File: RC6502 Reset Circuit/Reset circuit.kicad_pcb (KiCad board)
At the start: 2 copper layers, 99.1 x 33 mm, 12 parts, among them J1 CONN_01X39, J2 XTAL Enable, SW1 RESET, U1 NE555, U2 74LS04, X1 1MHz

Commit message: Exported files
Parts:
- added C4: 100nF, Capacitors_THT:C_Disc_D3.0mm_W1.6mm_P2.50mm, F.Cu at (119.4, 139.1)
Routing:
- net VCC: track 149.8 -> 178.2 mm
- net GND: track 155.0 -> 158.1 mm
- net RESET: track 81.2 -> 83.5 mm

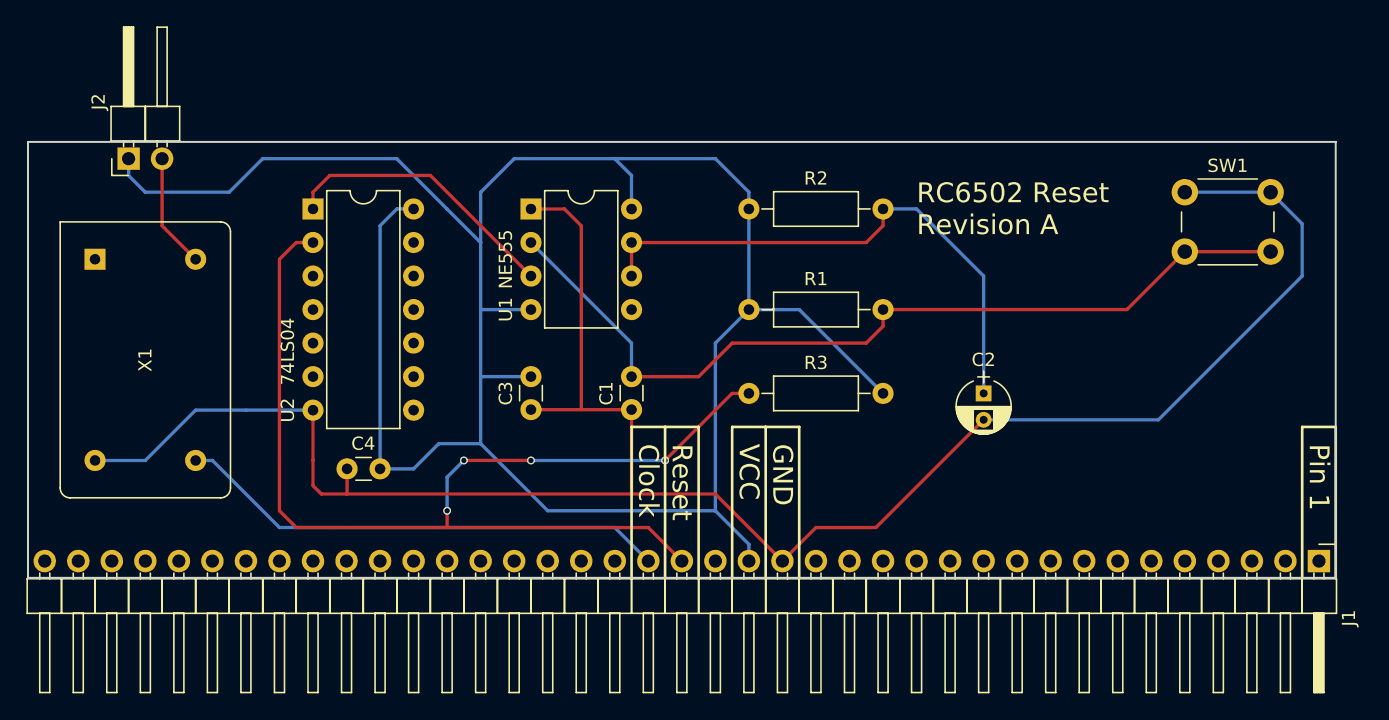
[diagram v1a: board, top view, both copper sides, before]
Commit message: Reset circuit revision B
Fixed floating inputs on hex inverter (needed when using HCT), added 74HCT74 in order to allow clock division by 2 and 4 (in case missing matching TTL quartz crystal or want even slower clock than stock).
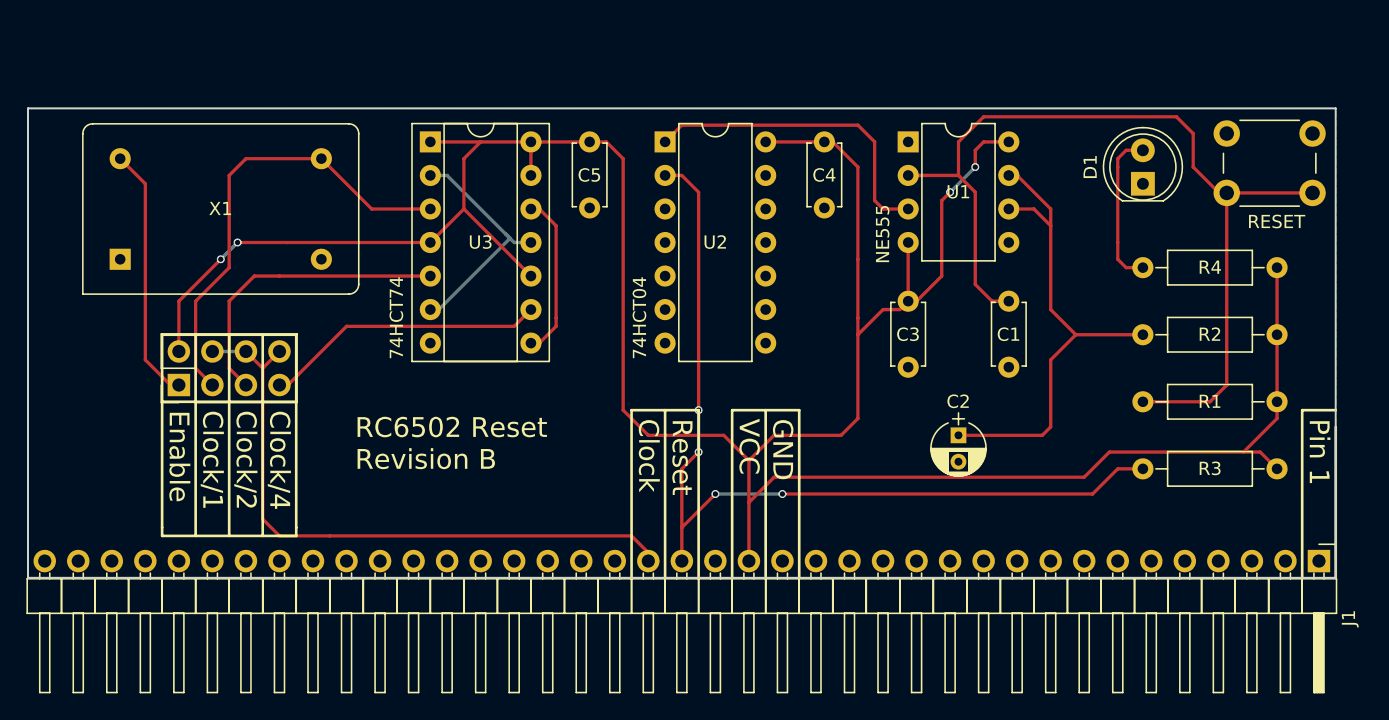
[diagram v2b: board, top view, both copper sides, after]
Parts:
- added C5: 100nF, Capacitors_THT:C_Disc_D4.7mm_W2.5mm_P5.00mm, F.Cu at (135.3, 114.3)
- added D1: Power, LEDs:LED_D5.0mm, F.Cu at (177.2, 117.5)
- added R4: 330, Resistors_THT:R_Axial_DIN0207_L6.3mm_D2.5mm_P10.16mm_Horizontal, F.Cu at (187.3, 123.8)
- added U3: 74HCT74, Housings_DIP:DIP-14_W7.62mm_Socket, F.Cu at (123.2, 114.3)
- C1, C3, C4: footprint Capacitors_THT:C_Disc_D3.0mm_W1.6mm_P2.50mm -> Capacitors_THT:C_Disc_D4.7mm_W2.5mm_P5.00mm
- J2: value XTAL Enable -> CONN_02X04; footprint Pin_Headers:Pin_Header_Angled_1x02_Pitch2.54mm -> Pin_Headers:Pin_Header_Straight_2x04_Pitch2.54mm
- U2: value 74LS04 -> 74HCT04
- moved C4 41.8 mm to (153.0, 114.3), turned to 270 degrees
- moved R2 41.1 mm to (187.3, 128.9), turned to 180 degrees
- moved R1 40.6 mm to (187.3, 134.0), turned to 180 degrees
- moved R3 30.4 mm to (177.2, 139.1)
- moved C1 29.1 mm to (167.0, 126.4)
- moved C3 29.1 mm to (159.4, 126.4)
- moved U1 29.0 mm to (159.4, 114.3)
- moved U2 27.1 mm to (141.0, 114.3)
- moved J2 17.6 mm to (104.1, 132.7)
- moved SW1 5.46 mm to (183.5, 113.7)
- moved C2 3.70 mm to (163.2, 136.5)
- moved X1 1.90 mm to (99.7, 123.2), turned to 0 degrees
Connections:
- J2 pad 1: VCC -> Net-(J2-Pad1)
- J2 pad 2: Net-(J2-Pad2) -> VCC
- U2 pad 11: (no net) -> GND
- U2 pad 13: (no net) -> GND
- U2 pad 3: (no net) -> GND
- U2 pad 5: (no net) -> GND
- U2 pad 9: (no net) -> GND
- X1 pad 14: Net-(J2-Pad2) -> Net-(J2-Pad1)
- X1 pad 8: CLOCK -> CLOCK/1
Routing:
- net GND: track 158.1 -> 0.00 mm
- net VCC: track 178.2 -> 216.1 mm, vias 0 -> 4
- net CLOCK/1: track 0.00 -> 34.8 mm
- net CLOCK/2: track 0.00 -> 22.9 mm
- net CLOCK/4: track 0.00 -> 21.4 mm
- net Net-(J2-Pad1): track 0.00 -> 19.4 mm
- net Net-(U3-Pad11): track 0.00 -> 18.4 mm
- net RESET: track 83.5 -> 68.3 mm
- net Net-(D1-Pad2): track 0.00 -> 12.6 mm
- net Net-(U3-Pad12): track 0.00 -> 12.5 mm
- net CLOCK: track 37.4 -> 48.5 mm
- net Net-(J2-Pad2): track 8.67 -> 0.00 mm
- net Net-(C1-Pad1): track 66.4 -> 71.1 mm
- net Net-(C2-Pad1): track 42.0 -> 38.3 mm
- net Net-(U1-Pad3): track 21.5 -> 24.2 mm
- added copper zone on B.Cu, net GND
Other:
- board size 99.1 x 33 mm -> 99.1 x 35.6 mm
- board text added: "Clock/1"
- board text added: "Clock/2"
- board text added: "Clock/4"
- board text added: "Enable"
- board text added: "RC6502 Reset Revision B"
- board text removed: "RC6502 Reset Revision A"
